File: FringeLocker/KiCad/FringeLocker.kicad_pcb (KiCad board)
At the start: 2 copper layers, 62.2 x 54.9 mm, 36 parts, among them J1 OUT, J2 TP Scaler, J3 Conn_01x03_Male, SW1 NIDEC_SS-10-16, SW2 SW_Push_DPDT, U1 TL074

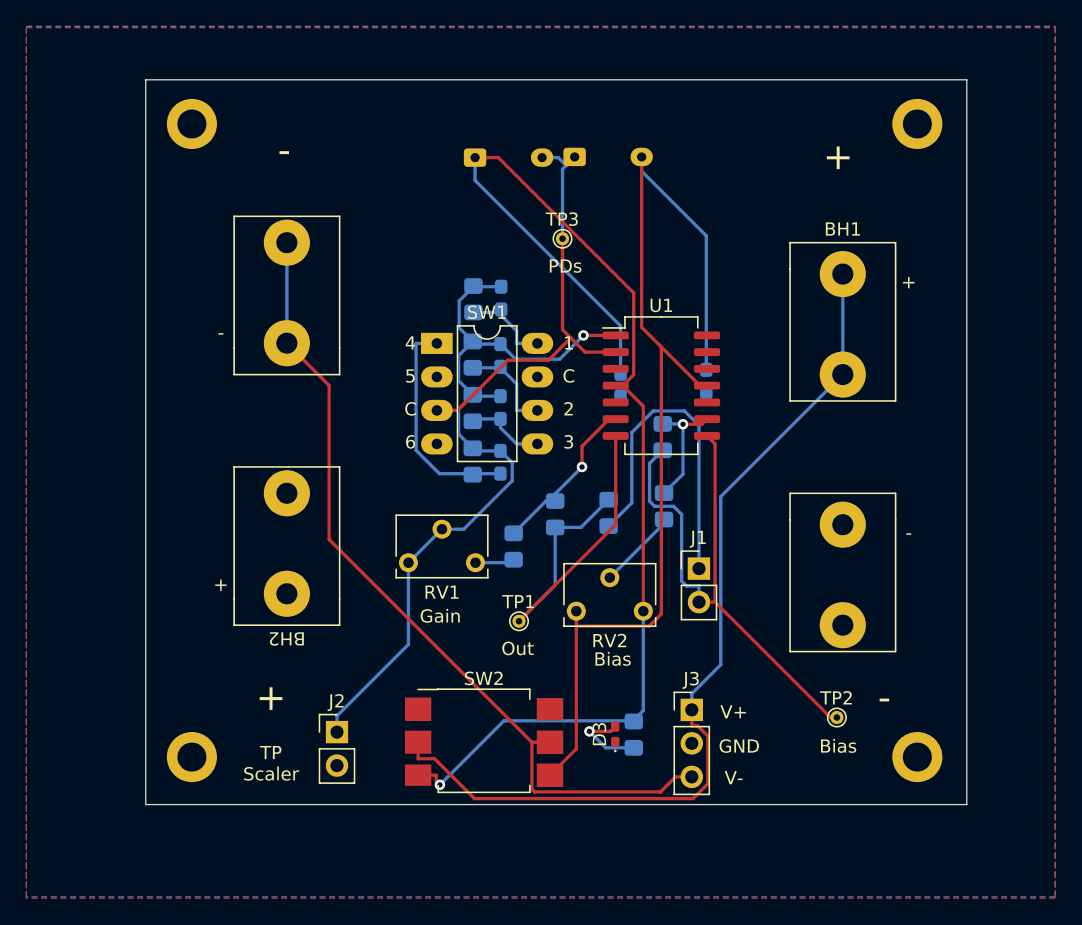
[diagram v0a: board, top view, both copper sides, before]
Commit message: V3.0
Added  a x10 gain stage and a 2nd order adjustable low pass filter
Removed battery holders, requires external +/-15V to +/-18V supply
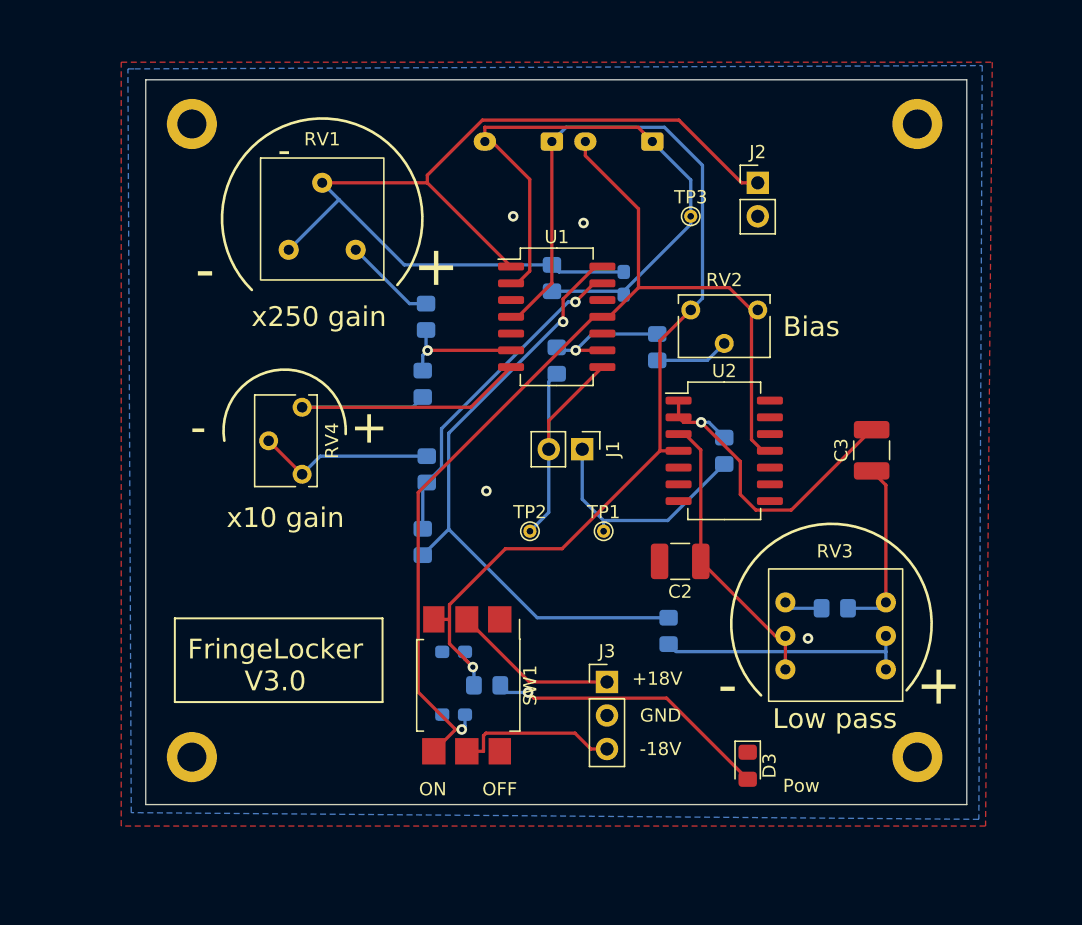
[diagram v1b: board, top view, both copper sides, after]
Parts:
- removed BH1, BH2: KeysTone_AAA, BatteryHolder:Keystone_AAA
- removed C4: 160nF, Capacitor_SMD:C_0603_1608Metric_Pad1.08x0.95mm_HandSolder
- removed SW2: SW_Push_DPDT, BatteryHolder:SlideSwitchASE_DPDT
- added R11: 1K, Resistor_SMD:R_0805_2012Metric_Pad1.20x1.40mm_HandSolder, B.Cu at (127.3, 82.7)
- added RV3: 3310H_001_102L, Bourns_3310H:Bourns3310H, F.Cu at (154.5, 97.9)
- added RV4: 10K, Potentiometer_THT:Potentiometer_Bourns_3266W_Vertical, F.Cu at (117.9, 83.1)
- added U2: TL074, Package_SO:SO-14_5.3x10.2mm_P1.27mm, F.Cu at (149.9, 81.3)
- C1: value 160pF -> 1.6nF
- C2: value 1.6nF -> 10uF; footprint Capacitor_SMD:C_0603_1608Metric_Pad1.08x0.95mm_HandSolder -> Capacitor_SMD:C_1210_3225Metric_Pad1.33x2.70mm_HandSolder; moved to F.Cu
- C3: value 16nF -> 10uF; footprint Capacitor_SMD:C_0603_1608Metric_Pad1.08x0.95mm_HandSolder -> Capacitor_SMD:C_1210_3225Metric_Pad1.33x2.70mm_HandSolder; moved to F.Cu
- D3: footprint LED_SMD:LED_0402_1005Metric_Pad0.77x0.64mm_HandSolder -> LED_SMD:LED_0805_2012Metric_Pad1.15x1.40mm_HandSolder
- R10: value 10K -> 7.5K
- R2: value 22K -> 250K
- R7: value 100K -> 200
- R8: value 10K -> 200
- R9: value 1K -> 10K
- RV1: value 10K -> 3310Y_001_503L; footprint Potentiometer_THT:Potentiometer_Bourns_3266W_Vertical -> Bourns_3310H:Bourns3310Y
- SW1: value NIDEC_SS-10-16 -> SW_Push_DPDT; footprint BatteryHolder:NIDEC_SS-10-16 -> BatteryHolder:SlideSwitchASE_DPDT
- moved J2 52.5 mm to (152.4, 61.0)
- moved R7 33.5 mm to (158.2, 93.2), turned to 180 degrees
- moved C6 31.7 mm to (129.3, 101.3), turned to 180 degrees
- moved C3 28.3 mm to (161.0, 81.2), turned to 90 degrees
- moved TP2 27.2 mm to (135.1, 87.4)
- moved RV2 26.7 mm to (152.4, 70.6), turned to 0 degrees
- moved SW1 26.0 mm to (129.3, 99.1), turned to -90 degrees
- moved RV1 25.4 mm to (116.8, 66.0), turned to 0 degrees
- moved C5 23.9 mm to (129.3, 96.5), turned to 180 degrees
- moved R8 22.5 mm to (145.6, 94.9), turned to -90 degrees
- moved C2 20.7 mm to (146.5, 89.7), turned to 180 degrees
- moved R4 18.6 mm to (127.2, 71.1), turned to -90 degrees
- moved R2 14.1 mm to (127.0, 76.2)
- moved J1 12.7 mm to (139.1, 81.2), turned to -90 degrees
- moved R5 12.1 mm to (144.8, 73.4)
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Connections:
- C2 pad 1: Net-(C1-Pad1) -> Net-(C2-Pad1)
- C2 pad 2: Net-(C2-Pad2) -> GND
- C3 pad 1: Net-(C1-Pad1) -> Net-(C3-Pad1)
- D1 pad 2: Net-(D1-Pad2) -> Net-(C1-Pad2)
- D2 pad 1: Net-(D1-Pad2) -> Net-(C1-Pad2)
- J3 pad 1: Net-(BH1-Pad1) -> Net-(J3-Pad1)
- J3 pad 3: Net-(BH2-Pad3) -> Net-(J3-Pad3)
- R1 pad 1: Net-(R1-Pad1) -> Net-(C3-Pad2)
- R2 pad 2: Net-(R1-Pad1) -> Net-(R2-Pad2)
- R7 pad 1: Net-(C2-Pad2) -> Net-(C3-Pad1)
- R7 pad 2: Net-(C1-Pad1) -> Net-(R7-Pad2)
- R8 pad 1: Net-(C3-Pad2) -> Net-(R8-Pad1)
- R8 pad 2: Net-(C1-Pad1) -> Net-(R8-Pad2)
- R9 pad 1: Net-(C4-Pad2) -> Net-(R11-Pad2)
- R9 pad 2: Net-(C1-Pad1) -> Net-(R8-Pad1)
- SW1 pad 2: Net-(D1-Pad2) -> Net-(J3-Pad1)
- SW1 pad 3: unconnected-(SW1-Pad3) -> +15V
- SW1 pad 4: Net-(C4-Pad2) -> unconnected-(SW1-Pad4)
- SW1 pad 5: Net-(C3-Pad2) -> Net-(J3-Pad3)
- SW1 pad 6: Net-(C2-Pad2) -> -15V
- TP1 pad 1: Net-(R1-Pad1) -> Net-(J1-Pad1)
- TP3 pad 1: Net-(D1-Pad2) -> Net-(C1-Pad2)
- U1 pad 12: unconnected-(U1-Pad12) -> GND
- U1 pad 13: unconnected-(U1-Pad13) -> Net-(R11-Pad2)
- U1 pad 14: unconnected-(U1-Pad14) -> Net-(R8-Pad1)
- U1 pad 2: Net-(D1-Pad2) -> Net-(C1-Pad2)
- U1 pad 7: Net-(R1-Pad1) -> Net-(R2-Pad2)
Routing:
- net Net-(BH1-Pad1): track 69.1 -> 0.00 mm
- net Net-(BH2-Pad3): track 63.2 -> 0.00 mm
- net Net-(R8-Pad1): track 0.00 -> 47.4 mm, vias 0 -> 1
- net Net-(C1-Pad2): track 6.70 -> 48.2 mm
- net Net-(D1-Pad2): track 32.7 -> 0.00 mm
- net Net-(R1-Pad1): track 30.3 -> 0.00 mm
- net Net-(R2-Pad2): track 0.00 -> 26.6 mm
- net Net-(R11-Pad2): track 0.00 -> 24.9 mm, vias 0 -> 1
- net Net-(C2-Pad1): track 0.00 -> 21.9 mm
- net Net-(J1-Pad2): track 41.8 -> 20.7 mm
- net Net-(R8-Pad2): track 0.00 -> 19.3 mm
- net Net-(C3-Pad2): track 6.15 -> 25.0 mm, vias 0 -> 1
- net Net-(C4-Pad2): track 16.9 -> 0.00 mm
- net Net-(D3-Pad2): track 5.99 -> 21.7 mm
- net Net-(C1-Pad1): track 61.7 -> 77.3 mm, vias 1 -> 0
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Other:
- board text added: "+18V"
- board text added: "-18V"
- board text added: "FringeLocker V3.0"
- board text added: "Low pass"
- board text added: "OFF"
- board text added: "ON"
- board text added: "Pow"
- board text added: "x10 gain"
- board text added: "x250 gain"
- board text removed: "Gain"
- board text removed: "Out"
- board text removed: "PDs"
- board text removed: "TP Scaler"
- board text removed: "V+"
- board text removed: "V-"
- board text removed: "|<"
